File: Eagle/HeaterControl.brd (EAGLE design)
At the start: 25.7 x 38.1 mm, 37 parts, among them J1 JUMPER_SOLDER_1X2, Q1 P-FET

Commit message: Updated for r2 board
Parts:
- removed IO12: (no value), led:CHIP-LED0805
- removed J1: JUMPER_SOLDER_1X2, dp_devices:JUMPER_SOLDER_1X2
- removed R8: 10K, SparkFun-Resistors:0805
- added C4, C5: 0.1uF, SparkFun-Capacitors:0805-CAP
- added HEAT, IO0: (no value), led:CHIP-LED0805
- added R10: 1K, SparkFun-Resistors:0805
- added R11: 330, SparkFun-Resistors:0805
- moved R3 2.70 mm to (22.6, 15.2), turned to 270 degrees
- moved R2 0.57 mm to (20.3, 15.2), turned to 270 degrees
- moved R7 0.57 mm to (13.2, 7.62), turned to 270 degrees
- moved FLASH 0.06 mm to (8.70, 27.2)
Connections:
- removed net HEAT: Q1.1, R8.2
- removed net ICSPCLK: 10F320.3, R8.1, U$9.5
- new net N$6: Q1.1, R10.1
- new net N$7: HEAT.C, R7.2
- net 3V3: now also C4.1, C5.1, HEAT.A
- net GND: now also C4.2, C5.2, IO0.C; no longer IO12.C
- net IO0: now also R11.2
- net IO12: now also R10.2, R7.1; no longer R7.2
- net N$4: no longer J1.2
- net N$5: now also IO0.A, R11.1; no longer IO12.A, R7.1
- net REST: now also 10F320.3, U$9.5; no longer J1.1
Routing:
- net ICSPCLK: track 11.9 -> 0.00 mm
- net REST: track 24.8 -> 36.0 mm
- net N$4: track 14.2 -> 4.19 mm, vias 1 -> 0
- net IO0: track 1.81 -> 5.25 mm
- net IO12: track 4.50 -> 7.71 mm, vias 0 -> 1
- net N$6: track 0.00 -> 2.28 mm
- net 3V3: track 107.3 -> 109.6 mm, vias 1 -> 2
- net N$7: track 0.00 -> 2.11 mm
- net HEAT: track 1.98 -> 0.00 mm
- net N$11: track 15.6 -> 16.7 mm
- net N$5: track 1.61 -> 2.62 mm
- net N$3: track 12.4 -> 13.3 mm
- net N$9: track 13.1 -> 14.0 mm
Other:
- board text added: "PIC PWM"
- board text removed: "IO15 PWM"

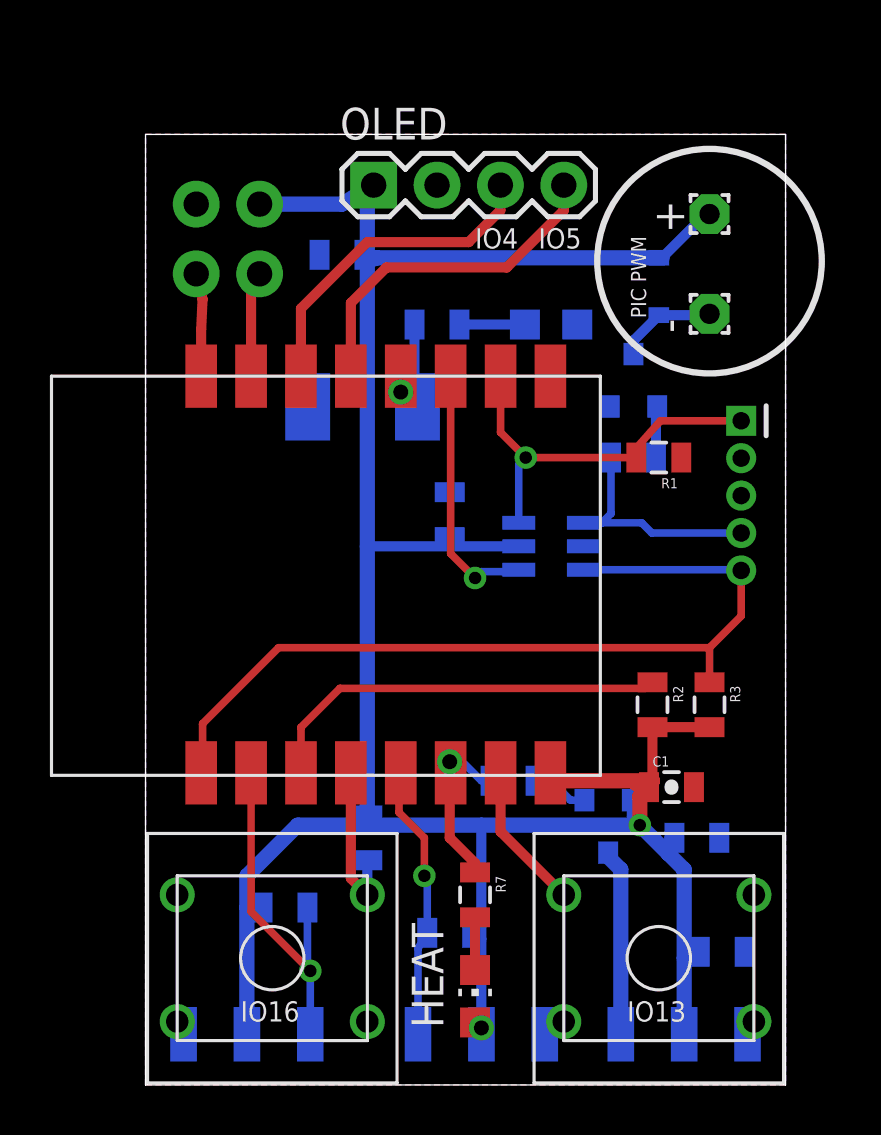
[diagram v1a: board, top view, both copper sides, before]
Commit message: Extended IO0, IO2 to side
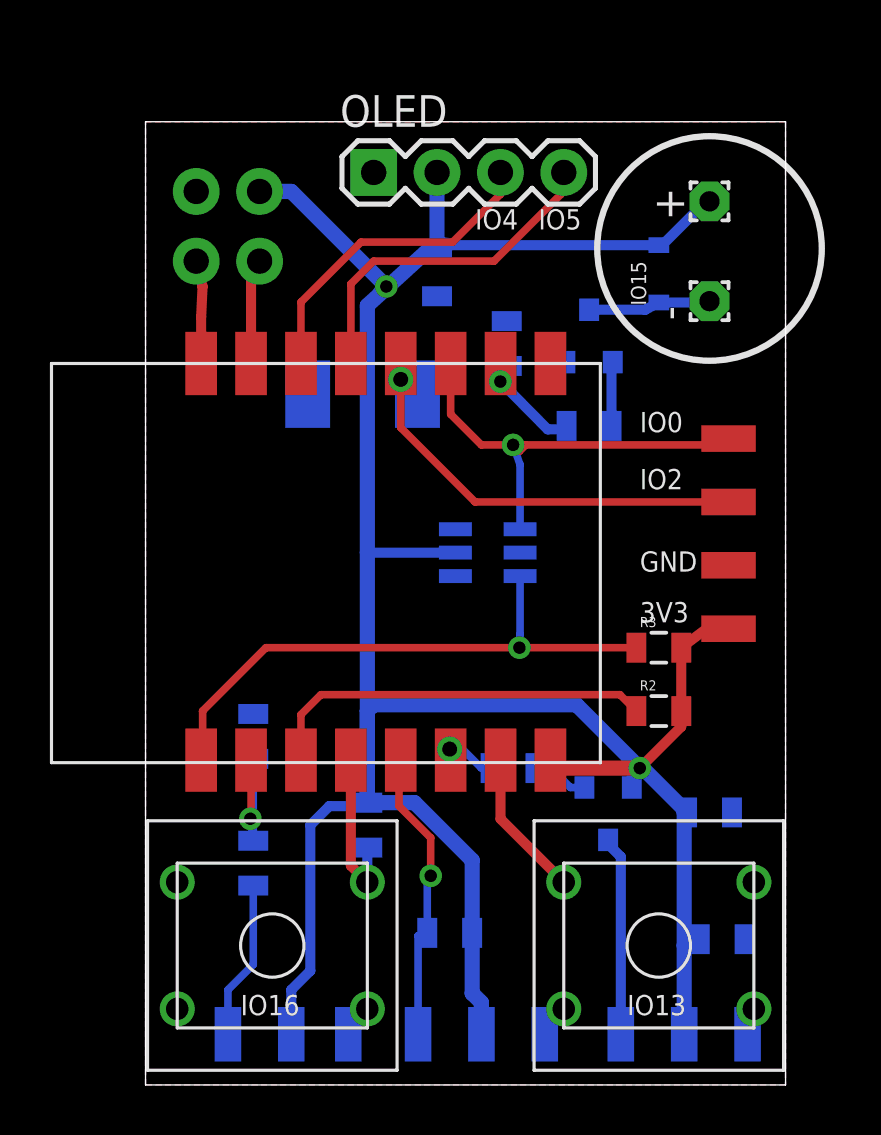
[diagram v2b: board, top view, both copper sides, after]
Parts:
- removed 10F320: PIC10F320T-I/OT, Microchip_By_element14_Batch_1:SOT95P270X145-6N
- removed C3, C5: 0.1uF, SparkFun-Capacitors:0805-CAP
- removed HEAT, IO0: (no value), led:CHIP-LED0805
- removed R7: 330, SparkFun-Resistors:0805
- added 10F: PIC10F202T-I/OT, Microchip_By_element14_Batch_1:SOT95P270X145-6N
- added U$12, U$13, U$14: SMD-PAD1, CuriousTech:SMD-PAD1
- C4: value 0.1uF -> 1uF
- R10: value 1K -> 10K
- R11: value 330 -> 4K7
- R6: value 4K7 -> 1K
- R9: value 10K -> 4K7
- U$9: value PIC-ICSP-MINI -> SMD-PAD1; device SparkFun-Connectors:PIC-ICSP-MINI -> CuriousTech:SMD-PAD1
- moved R6 21.1 mm to (17.8, 26.4), turned to 180 degrees
- moved R11 18.1 mm to (4.32, 14.0), turned to 90 degrees
- moved R5 13.3 mm to (14.7, 12.7), turned to 0 degrees
- moved R10 10.9 mm to (4.32, 8.89), turned to 90 degrees
- moved R1 7.62 mm to (14.5, 29.7), flipped to the bottom, turned to 270 degrees
- moved U$9 5.36 mm to (23.4, 18.3), turned to 0 degrees
- moved R9 5.04 mm to (12.2, 6.10), turned to 0 degrees
- moved R4 4.67 mm to (8.89, 10.4), turned to 90 degrees
- moved U$5 4.32 mm to (5.84, 2.03)
- moved U$4 4.06 mm to (8.13, 2.03), turned to 90 degrees
- moved C2 3.89 mm to (11.7, 32.5), turned to 270 degrees
- moved U$7 3.30 mm to (3.30, 2.03)
- moved R3 3.06 mm to (20.6, 17.5), turned to 0 degrees
- moved Q2 2.51 mm to (17.8, 30.0)
- moved C1 1.83 mm to (22.6, 10.9), flipped to the bottom, turned to 180 degrees
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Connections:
- net N$3 renamed SCL
- net N$9 renamed SDA
- removed net N$5: IO0.A, R11.1
- removed net PICPWM: 10F320.1, R5.1, U$9.4
- net 3V3: now also 10F.5, OLED.2, R9.1, U$5.>NAME, U$9.>NAME; no longer 10F320.5, C3.1, C5.1, HEAT.A, OLED.1, R6.1, R9.2, U$4.>NAME
- net ADC: now also R10.2, R11.1; no longer R4.1, U$7.>NAME
- net GND: now also 10F.2, OLED.1, R11.2, U$13.>NAME, U$4.>NAME; no longer 10F320.2, C3.2, C5.2, IO0.C, LEFT.P2, OLED.2, U$5.>NAME, U$9.3
- net IO0: now also U$14.>NAME; no longer R11.2
- net IO12: now also R5.2; no longer R10.2, R7.1
- net IO14: now also R9.2; no longer R6.2
- net IO15: now also R6.1; no longer 10F320.6, U$9.1
- net IO16: now also R4.1; no longer R9.1
- net IO2: now also 10F.1, U$12.>NAME; no longer 10F320.4
- net N$2: now also R6.2; no longer R5.2
- net N$6: now also R5.1; no longer R10.1
- net N$7: now also R10.1, U$7.>NAME; no longer HEAT.C, R7.2
- net REST: now also 10F.3; no longer 10F320.3, U$9.5
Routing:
- net IO0: track 5.25 -> 18.5 mm
- net REST: track 36.0 -> 24.4 mm, vias 0 -> 1
- net IO15: track 16.0 -> 4.94 mm
- net PICPWM: track 9.26 -> 0.00 mm
- net IO2: track 10.4 -> 17.9 mm
- net ADC: track 14.0 -> 7.05 mm
- net 3V3: track 109.6 -> 115.1 mm
- net IO12: track 7.71 -> 3.33 mm
- net N$7: track 2.11 -> 6.38 mm
- net N$5: track 2.62 -> 0.00 mm
- net IO14: track 11.1 -> 11.9 mm
- net N$11: track 16.7 -> 15.9 mm
- net N$4: track 4.19 -> 4.95 mm
- net N$1: track 7.49 -> 8.00 mm
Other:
- board size 25.7 x 38.1 mm -> 25.7 x 38.6 mm
- board text added: "3V3"
- board text added: "ADC"
- board text added: "CuriousTech.net"
- board text added: "ESP-07"
- board text added: "GND"
- board text added: "IO0"
- board text added: "IO15"
- board text added: "IO2"
- board text added: "Waterbed Heater"
- board text added: "WiFi Smart"
- board text removed: "CuriousTech.net Waterbed Heater"
- board text removed: "ESP-07/12"
- board text removed: "PIC PWM"
- board text removed: "Therm ADC"

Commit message: Added i2c to side for Am2320
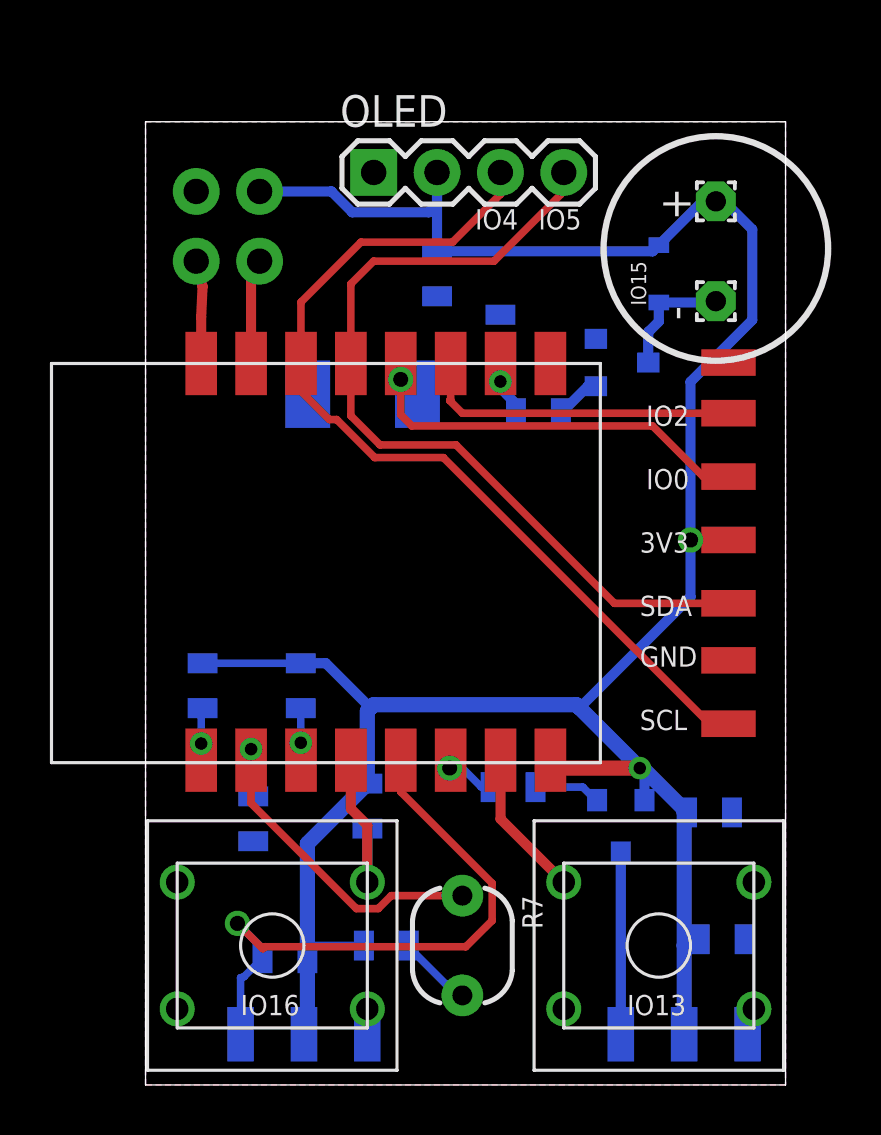
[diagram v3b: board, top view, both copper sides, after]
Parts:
- removed 10F: PIC10F202T-I/OT, Microchip_By_element14_Batch_1:SOT95P270X145-6N
- removed R11: 4K7, SparkFun-Resistors:0805
- removed U$5, U$7: SMD-PAD1, CuriousTech:SMD-PAD1
- added R7: PHOTOCELLPTH, SparkFun-Sensors:PHOTOCELL
- added R8: 1K, SparkFun-Resistors:0805
- added U$15, U$16: SMD-PAD1, CuriousTech:SMD-PAD1
- R10: value 10K -> 1K
- moved U$4 30.9 mm to (23.4, 29.0), flipped to the top, turned to 0 degrees
- moved R3 18.4 mm to (2.29, 16.0), flipped to the bottom, turned to 90 degrees
- moved R2 14.4 mm to (6.22, 16.0), flipped to the bottom, turned to 90 degrees
- moved U$10 7.11 mm to (3.81, 2.03)
- moved U$8 7.11 mm to (6.35, 2.03)
- moved U$11 7.11 mm to (8.89, 2.03)
- moved R9 6.68 mm to (5.59, 5.08)
- moved U$13 3.81 mm to (23.4, 17.0)
- moved U$9 3.56 mm to (23.4, 21.8)
- moved R6 2.09 mm to (15.7, 26.9)
- moved R10 1.78 mm to (4.32, 10.7)
- moved Q2 1.63 mm to (19.1, 29.0), turned to 90 degrees
- moved U$14 1.02 mm to (23.4, 24.4)
- moved U$12 1.02 mm to (23.4, 26.9)
- moved R4 0.76 mm to (8.89, 11.2)
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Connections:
- removed net N$7: R10.1, U$7.>NAME
- new net N$5: R7.2, R8.1
- net 3V3: now also R8.2; no longer 10F.5, U$5.>NAME
- net ADC: now also R7.1; no longer R11.1
- net GND: now also R10.1; no longer 10F.2, R11.2
- net IO2: no longer 10F.1
- net REST: no longer 10F.3
- net SCL: now also U$15.>NAME
- net SDA: now also U$16.>NAME
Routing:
- net SCL: track 13.1 -> 37.1 mm
- net REST: track 24.4 -> 2.11 mm
- net SDA: track 14.0 -> 34.3 mm
- net N$11: track 15.9 -> 2.18 mm, vias 0 -> 1
- net IO14: track 11.9 -> 24.3 mm
- net 3V3: track 115.1 -> 103.2 mm
- net ADC: track 7.05 -> 14.6 mm
- net N$7: track 6.38 -> 0.00 mm
- net IO2: track 17.9 -> 12.9 mm, vias 1 -> 0
- net N$5: track 0.00 -> 3.02 mm
- net IO15: track 4.94 -> 3.28 mm
- net IO12: track 3.33 -> 2.29 mm
- net IO16: track 6.55 -> 7.31 mm
- net N$1: track 8.00 -> 7.28 mm
- net N$2: track 2.56 -> 1.85 mm
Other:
- board text added: "SCL"
- board text added: "SDA"

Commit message: Added top buttons
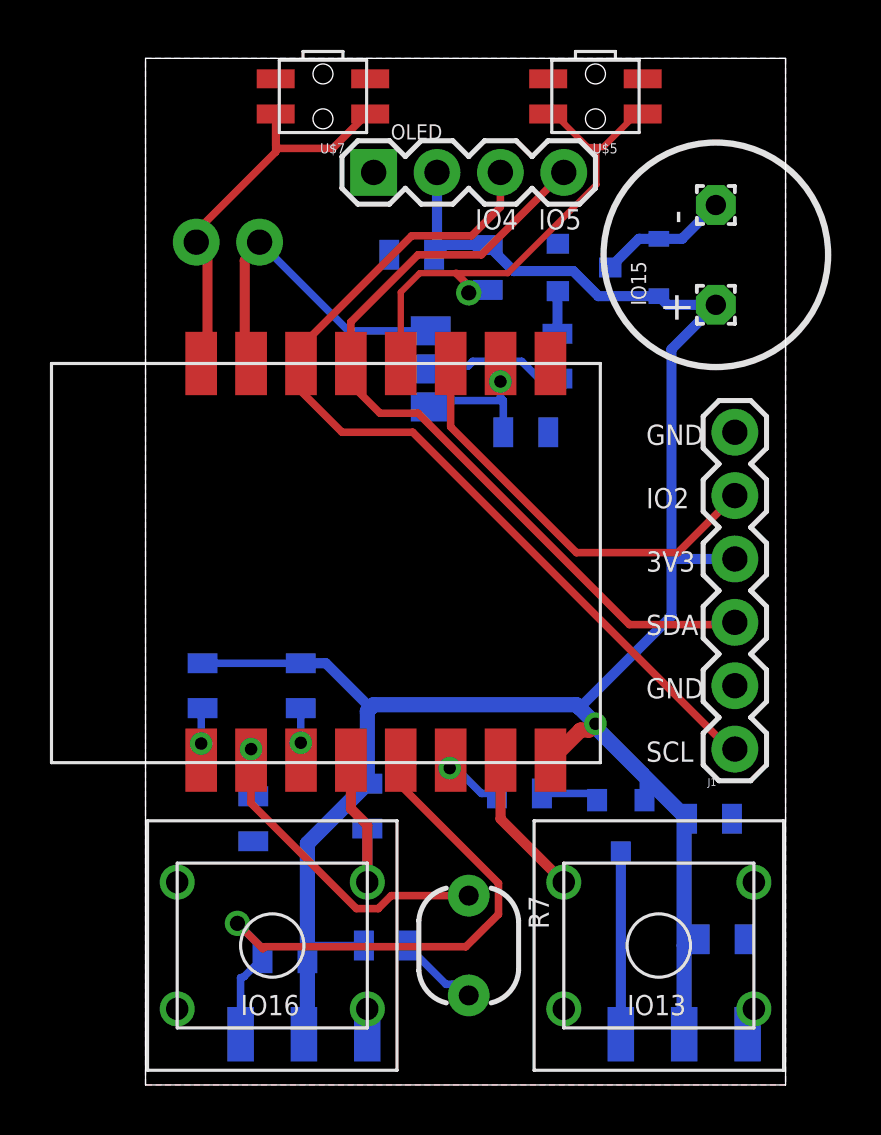
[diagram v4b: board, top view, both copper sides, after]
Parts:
- removed +__-: (no value), SparkFun-Connectors:1X02
- removed FLASH: BTN_4MM, CuriousTech:BTN_4MM
- removed U$12, U$13, U$14, U$15, U$16, U$4, U$9: SMD-PAD1, CuriousTech:SMD-PAD1
- added J1: (no value), SparkFun-Connectors:1X06
- added R11: 10K, SparkFun-Resistors:0805
- added SJ1: (no value), jumper:SJ_2
- added U$5, U$7: SIDE-TACT, CuriousTech:SIDE-TACT
- moved + 4.15 mm to (22.9, 31.3)
- moved Q2 4.10 mm to (17.5, 32.8)
- moved R1 3.94 mm to (15.2, 26.2), turned to 0 degrees
- moved - 3.85 mm to (22.9, 35.3)
- moved R6 2.41 mm to (16.5, 29.2), turned to 90 degrees
- moved C2 1.27 mm to (10.7, 33.3), turned to 0 degrees
- moved . 0.76 mm to (2.03, 33.8)
- moved R5 0.36 mm to (15.0, 11.7)
- moved C1 0.25 mm to (22.6, 10.7)
- moved R7 0.25 mm to (13.0, 5.59)
- moved D1 0.25 mm to (20.6, 32.8), turned to 90 degrees
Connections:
- new net N$8: R6.1, SJ1.2
- net 3V3: now also J1.4, R11.1; no longer +__-.1, U$9.>NAME
- net GND: now also J1.2, J1.6, U$5.3, U$5.4, U$7.3, U$7.4; no longer +__-.2, FLASH.1, U$13.>NAME, U$4.>NAME
- net IO0: now also R11.2, U$5.1, U$5.2; no longer FLASH.2, U$14.>NAME
- net IO15: now also SJ1.3; no longer R6.1
- net IO2: now also J1.5; no longer U$12.>NAME
- net RXD: now also SJ1.1
- net SCL: now also J1.1; no longer U$15.>NAME
- net SDA: now also J1.3; no longer U$16.>NAME
- net TXD: now also U$7.1, U$7.2
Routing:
- net TXD: track 4.13 -> 17.3 mm
- net 3V3: track 103.2 -> 91.4 mm, vias 2 -> 1
- net RXD: track 4.22 -> 13.5 mm
- net N$8: track 0.00 -> 5.49 mm
- net IO2: track 12.9 -> 17.0 mm
- net IO0: track 18.1 -> 20.7 mm
- net IO15: track 3.28 -> 5.83 mm
- net SDA: track 34.3 -> 32.9 mm
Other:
- board size 25.7 x 38.6 mm -> 25.7 x 41.1 mm
- board text removed: "IO0"
